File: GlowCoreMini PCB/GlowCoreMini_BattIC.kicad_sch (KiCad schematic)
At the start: 13 parts, among them U3 PTVSHC3N12VU

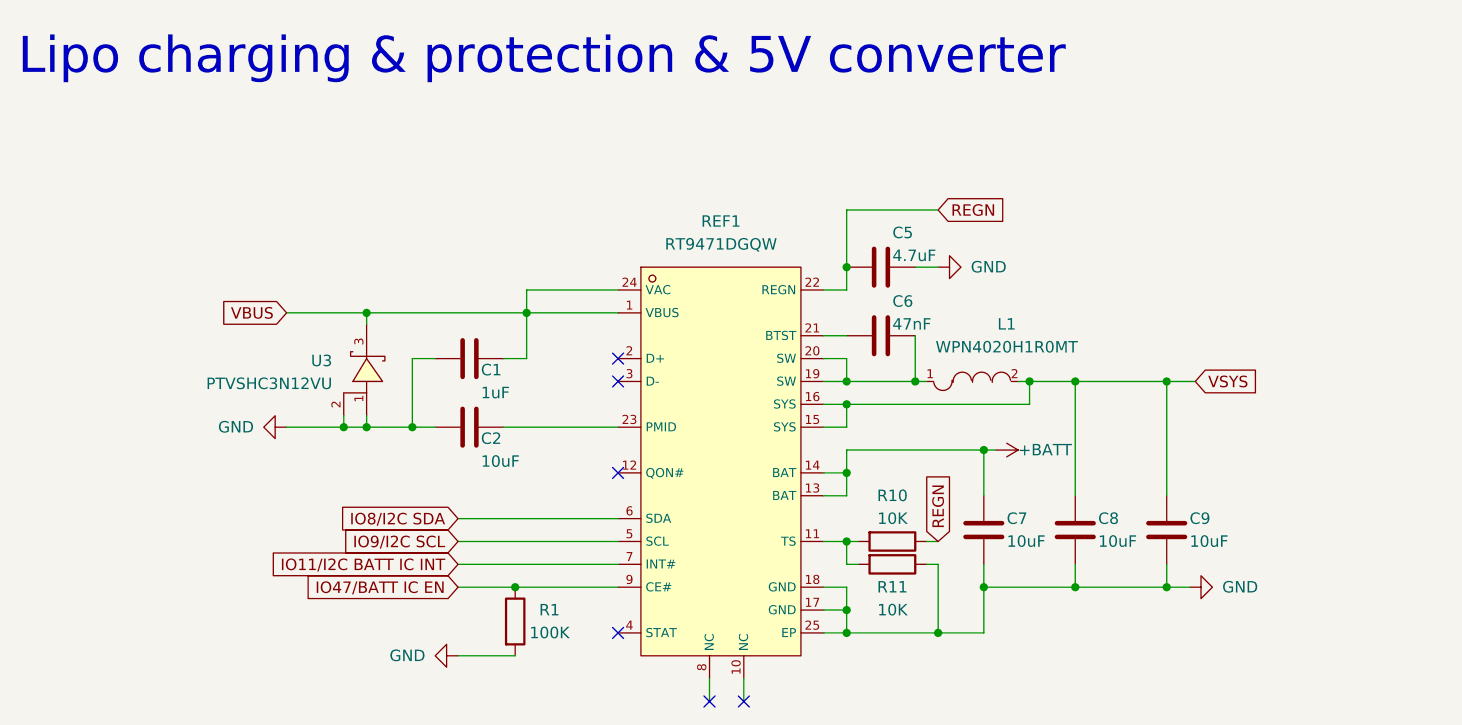
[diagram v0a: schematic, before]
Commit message: split up schematic
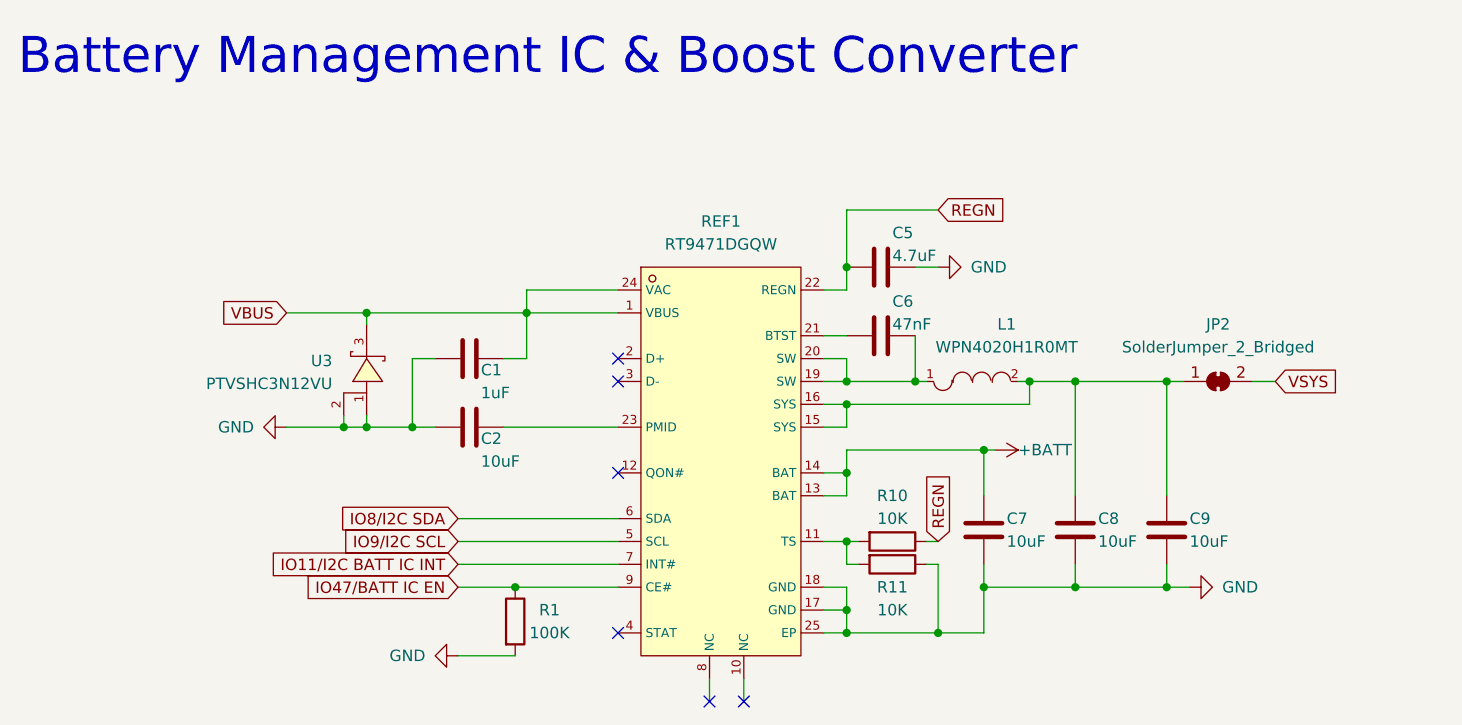
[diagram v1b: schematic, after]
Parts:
- added JP2: SolderJumper_2_Bridged, Jumper:SolderJumper-2_P1.3mm_Bridged_RoundedPad1.0x1.5mm, symbol Jumper:SolderJumper_2_Bridged
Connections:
- net VSYS: now also JP2.2 (B); no longer C8.2, C9.2, L1.2, REF1.15 (SYS), REF1.16 (SYS)
- new net: C8.2, C9.2, JP2.1 (A), L1.2, REF1.15 (SYS), REF1.16 (SYS)
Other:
- note added: "Battery Management IC & Boost Converter"
- note removed: "Lipo charging & protection & 5V converter"
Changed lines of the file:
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@@
   (junction (at 118.745 60.96) (diameter 0) (color 0 0 0 0)
   )
+  (junction (at 146.685 60.96) (diameter 0) (color 0 0 0 0)
+  )
   (junction (at 57.785 66.04) (diameter 0) (color 0 0 0 0)
-  )
-  (junction (at 146.685 60.96) (diameter 0) (color 0 0 0 0)
   )
   (junction (at 146.685 83.82) (diameter 0) (color 0 0 0 0)
@@
     (stroke (width 0) (type default))
   )
+  (wire (pts (xy 158.75 60.96) (xy 156.21 60.96))
+    (stroke (width 0) (type default))
+  )
   (wire (pts (xy 136.525 83.82) (xy 146.685 83.82))
     (stroke (width 0) (type default))
@@
     (stroke (width 0) (type default))
   )
+  (wire (pts (xy 146.685 60.96) (xy 148.59 60.96))
+    (stroke (width 0) (type default))
+  )
   (wire (pts (xy 126.365 68.58) (xy 126.365 73.66))
     (stroke (width 0) (type default))
@@
     (stroke (width 0) (type default))
   )
-  (wire (pts (xy 146.685 60.96) (xy 149.86 60.96))
-    (stroke (width 0) (type default))
-  )
   (wire (pts (xy 130.175 60.96) (xy 131.445 60.96))
     (stroke (width 0) (type default))
@@
     (stroke (width 0) (type default))
   )
-  (text "Lipo charging & protection & 5V converter" (at 19.05 27.305 0)
+  (text "Battery Management IC & Boost Converter" (at 19.05 27.305 0)
     (effects (font (size 4 4)) (justify left bottom))
   )
@@
     )
   )
-  (global_label "VSYS" (shape input) (at 149.86 60.96 0) (fields_autoplaced)
+  (global_label "VSYS" (shape input) (at 158.75 60.96 0) (fields_autoplaced)
     (effects (font (size 1.27 1.27)) (justify left))
-    (property "Intersheetrefs" "${INTERSHEET_REFS}" (at 157.362 60.96 0)
+    (property "Intersheetrefs" "${INTERSHEET_REFS}" (at 166.252 60.96 0)
       (effects (font (size 1.27 1.27)) (justify left) hide)
     )
@@
         )
       )
+    )
+  )
+  (symbol (lib_id "Jumper:SolderJumper_2_Bridged") (at 152.4 60.96 0) (unit 1)
+    (in_bom yes) (on_board yes) (dnp no) (fields_autoplaced)
+    (property "Reference" "JP2" (at 152.4 54.61 0)
+      (effects (font (size 1.27 1.27)))
+    )
+    (property "Value" "SolderJumper_2_Bridged" (at 152.4 57.15 0)
+      (effects (font (size 1.27 1.27)))
+    )
+    (property "Footprint" "Jumper:SolderJumper-2_P1.3mm_Bridged_RoundedPad1.0x1.5mm" (at 152.4 60.96 0)
+      (effects (font (size 1.27 1.27)) hide)
+    )
+    (property "Datasheet" "~" (at 152.4 60.96 0)
+      (effects (font (size 1.27 1.27)) hide)
+    )
+    (pin "1")
+    (pin "2")
+    (instances
+      (project "GlowCoreMini PCB"
+        (path "/c6f71574-e06f-4ae6-b347-b6a4861b944a/b7f3bf05-da0f-4528-9622-2564946510a6"
+          (reference "JP2") (unit 1)
+        )
+      )
